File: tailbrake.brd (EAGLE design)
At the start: 88.9 x 120.7 mm, 60 parts, among them J1 POWER, Q1 2N2222, Q2 2N2222, Q3 2N2222, Q4 2N2222, U1 CL2N3, U10 CL2N3, U11 CL2N3, U12 CL2N3, U2 CL2N3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

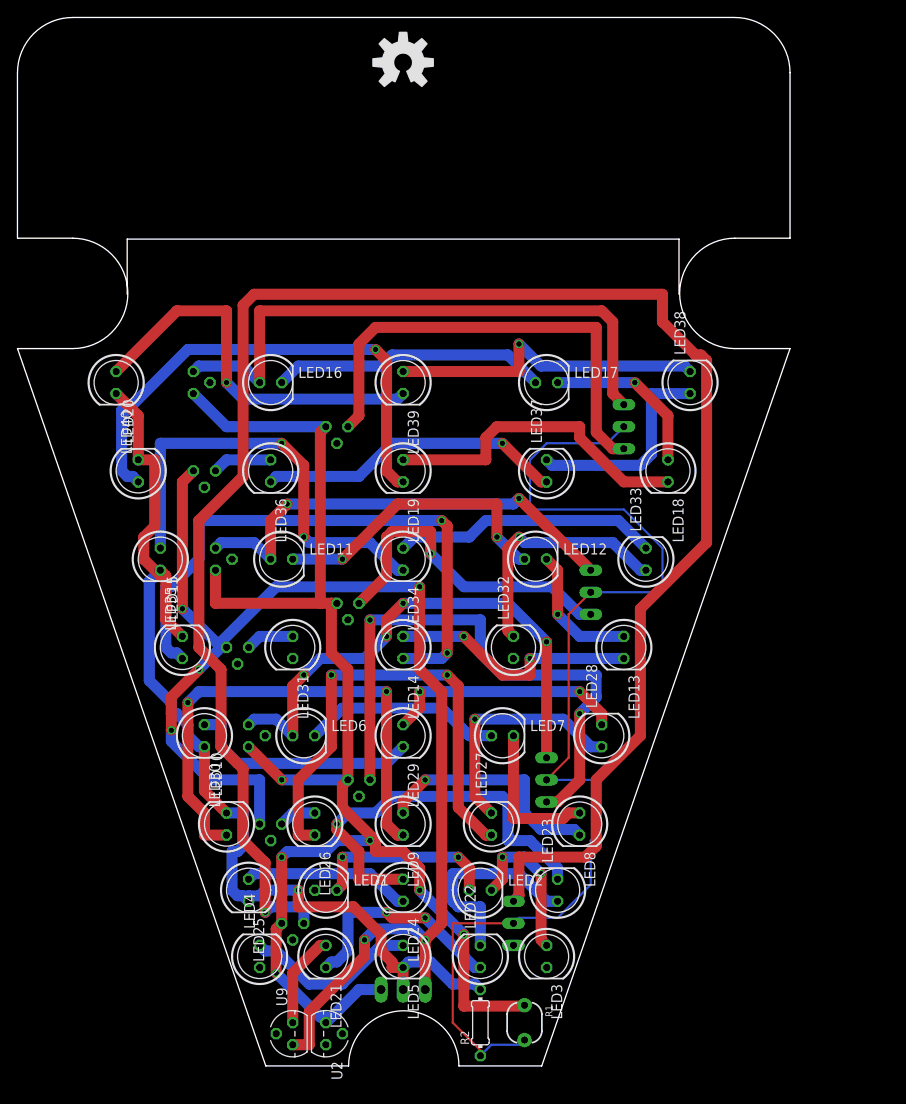
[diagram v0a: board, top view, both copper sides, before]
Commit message: Final version, so far - brought tail/brake to ready for manufacture - two assembly versions: simple and dimmed - sorted top/bottom silk, added branding and extra artwork
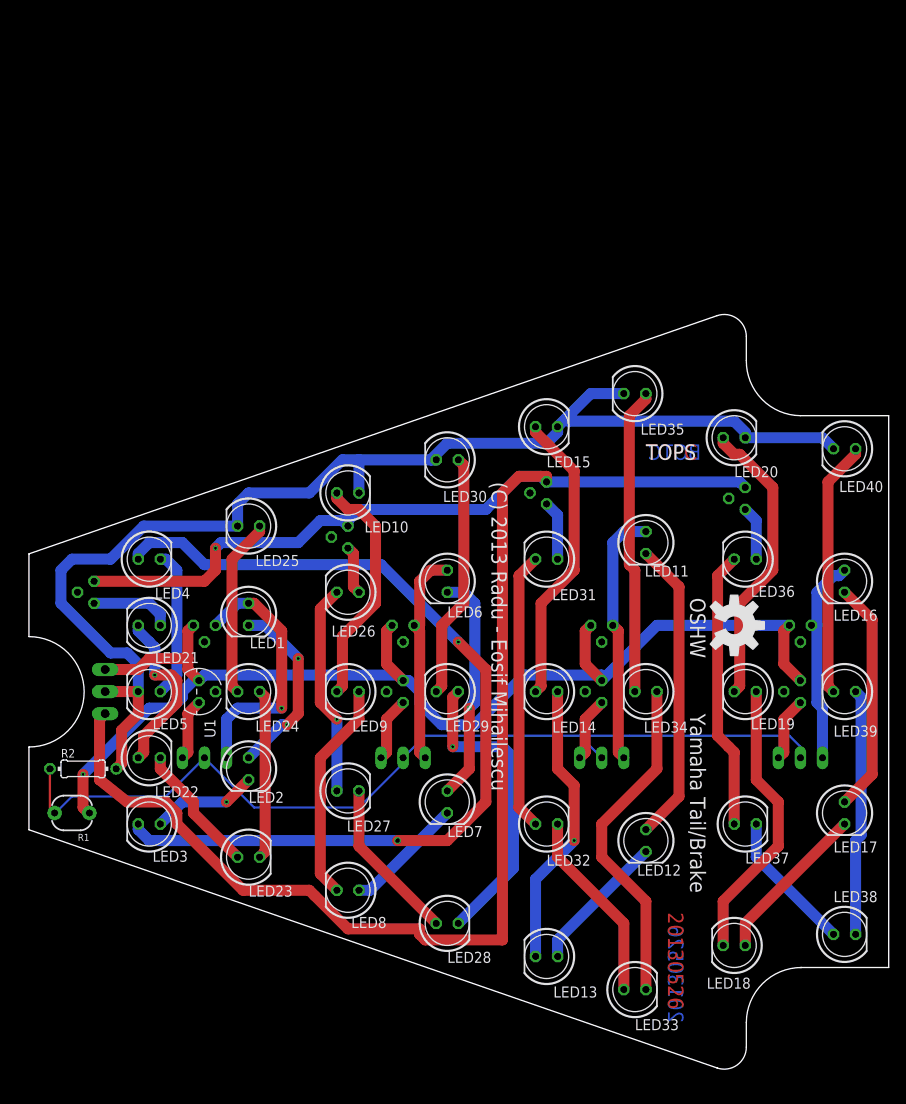
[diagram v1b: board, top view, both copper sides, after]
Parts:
- moved LED40 84.2 mm to (94.0, 72.4), turned to 180 degrees
- moved U8 75.2 mm to (88.9, 52.1), turned to 180 degrees
- moved LOGO1 75.1 mm to (81.3, 52.1), turned to 270 degrees
- moved LED16 69.9 mm to (94.0, 57.1), turned to 270 degrees
- moved LED20 68.7 mm to (81.3, 73.7), turned to 0 degrees
- moved LED38 65.9 mm to (94.0, 16.5), turned to 0 degrees
- moved U12 62.3 mm to (82.5, 66.7), turned to 270 degrees
- moved LED39 62.0 mm to (94.0, 44.5), turned to 180 degrees
- moved U7 61.4 mm to (88.9, 44.5), turned to 270 degrees
- moved LED17 60.2 mm to (94.0, 30.5), turned to 270 degrees
- moved LED35 57.8 mm to (69.8, 78.7), turned to 180 degrees
- moved R1 57.4 mm to (5.08, 30.5), turned to 180 degrees
- moved U9 55.7 mm to (7.62, 55.9), flipped to the bottom, turned to 270 degrees
- moved LED36 55.5 mm to (82.5, 59.7), turned to 180 degrees
- moved LED18 55.1 mm to (81.3, 15.2), turned to 180 degrees
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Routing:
- net N$6: track 216.5 -> 7.14 mm, vias 1 -> 0
- net N$3: track 0.00 -> 105.5 mm, vias 0 -> 2
- net N$7: track 67.0 -> 7.40 mm, vias 2 -> 0
- net TAIL: track 153.0 -> 203.6 mm, vias 6 -> 1
- net N$24: track 54.2 -> 7.40 mm
- net N$22: track 68.1 -> 24.8 mm
- net N$11: track 61.3 -> 25.2 mm, vias 4 -> 0
- net N$18: track 67.8 -> 34.2 mm, vias 2 -> 0
- net BRAKE: track 172.3 -> 139.3 mm, vias 6 -> 1
- net N$12: track 59.6 -> 27.3 mm, vias 2 -> 0
- net N$36: track 0.00 -> 32.1 mm
- net N$31: track 56.1 -> 24.4 mm, vias 2 -> 1
- net N$13: track 38.1 -> 7.40 mm, vias 1 -> 0
- net N$4: track 0.00 -> 30.2 mm, vias 0 -> 1
- net N$28: track 46.5 -> 19.6 mm, vias 1 -> 0
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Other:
- board size 88.9 x 120.7 mm -> 98.9 x 86.8 mm
- board text added: "(C) 2013 Radu - Eosif Mihailescu"
- board text added: "20130526"
- board text added: "B"
- board text added: "BOTC"
- board text added: "BOTS"
- board text added: "OSHW"
- board text added: "T"
- board text added: "TOPC"
- board text added: "TOPS"
- board text added: "Yamaha Tail/Brake"
